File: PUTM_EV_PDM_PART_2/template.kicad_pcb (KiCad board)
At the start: 4 copper layers, 60 x 100 mm, 10 parts, among them J2 UPS-08-07.0-01-L-V, J3 Conn_02x18_Counter_Clockwise, J4 Conn_01x06, J5 +24V OUT, J7 UPS-08-07.0-01-L-V, J8 +24V IN

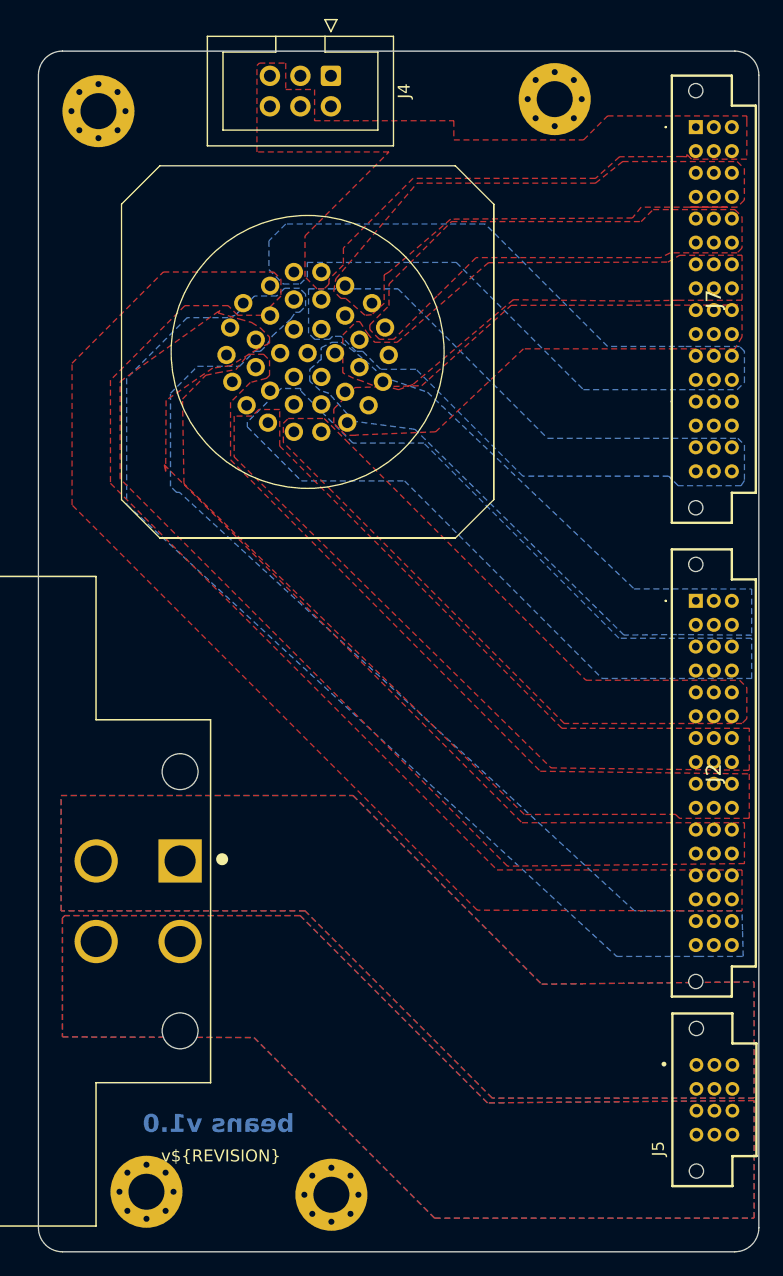
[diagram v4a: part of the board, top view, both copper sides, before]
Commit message: Add files via upload
Fixed fan and pump routing, fixed spacing between internal connectors to fit PDM
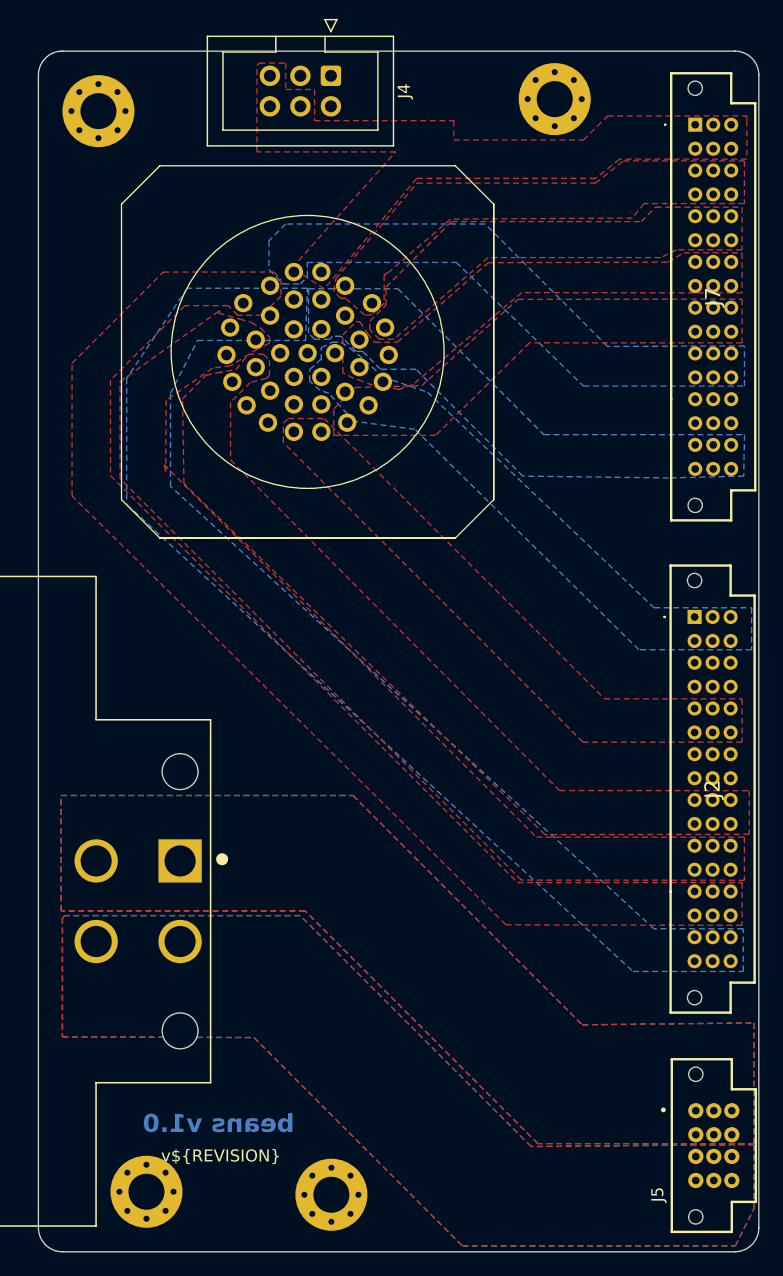
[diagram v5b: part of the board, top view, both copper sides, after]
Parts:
- J5: footprint UPS-02-04.0-01-L-V:SAMTEC_UPS-02-04.0-01-L-V -> UPS-02-07.0-01-L-V:SAMTEC_UPS-02-XX.X-X-X-V
- moved J5 3.82 mm to (153.8, 121.2)
- moved J2 1.35 mm to (153.7, 77.1)
- moved J7 0.21 mm to (153.7, 36.1)
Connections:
- J2 pad B1: /PUMP_1 -> Net-(J2-PadB1)
- J2 pad B2: /PUMP_1 -> Net-(J2-PadB1)
- J2 pad B3: /PUMP_1 -> Net-(J2-PadB1)
- J2 pad B4: /PUMP_1 -> Net-(J2-PadB1)
- J2 pad B5: /PUMP_1 -> Net-(J2-PadB1)
- J2 pad B6: /PUMP_1 -> Net-(J2-PadB1)
- J2 pad D1: /PUMP_2 -> Net-(J2-PadD1)
- J2 pad D2: /PUMP_2 -> Net-(J2-PadD1)
- J2 pad D3: /PUMP_2 -> Net-(J2-PadD1)
- J2 pad D4: /PUMP_2 -> Net-(J2-PadD1)
- J2 pad D5: /PUMP_2 -> Net-(J2-PadD1)
- J2 pad D6: /PUMP_2 -> Net-(J2-PadD1)
- J3 pad 11: /PUMP_2 -> /FAN
- J3 pad 2: /REARBOX 1 24VDC -> /PUMP_1
- J3 pad 23: /FAN -> unconnected-(J3-Pin_23-Pad23)
- J3 pad 3: /REARBOX 1 24VDC -> /PUMP_1
- J3 pad 7: /REARBOX 3 24VDC -> /PUMP_2
- J3 pad 8: /REARBOX 3 24VDC -> /PUMP_2
- J7 pad B1: /REARBOX 1 24VDC -> /PUMP_1
- J7 pad B2: /REARBOX 1 24VDC -> /PUMP_1
- J7 pad B3: /REARBOX 1 24VDC -> /PUMP_1
- J7 pad B4: /REARBOX 1 24VDC -> /PUMP_1
- J7 pad B5: /REARBOX 1 24VDC -> /PUMP_1
- J7 pad B6: /REARBOX 1 24VDC -> /PUMP_1
- J7 pad E1: /REARBOX 3 24VDC -> /PUMP_2
- J7 pad E2: /REARBOX 3 24VDC -> /PUMP_2
- J7 pad E3: /REARBOX 3 24VDC -> /PUMP_2
- J7 pad E4: /REARBOX 3 24VDC -> /PUMP_2
- J7 pad E5: /REARBOX 3 24VDC -> /PUMP_2
- J7 pad E6: /REARBOX 3 24VDC -> /PUMP_2
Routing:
- added copper zone on F.Cu, net /PUMP_1
- removed copper zone on B.Cu, net /PUMP_1
- removed copper zone on F.Cu, net /REARBOX 1 24VDC
- removed copper zone on F.Cu, net /REARBOX 3 24VDC
